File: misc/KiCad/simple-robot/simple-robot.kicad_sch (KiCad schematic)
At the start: 70 parts, among them J1 MotLA, J10 Screw_Terminal_2_P5.00mm, J11 JST02 HC-SR04, J12 IR_RF, J13 IR_LF, J14 JST_GV, J15 JST RF_Logic, J16 JST RF_PWR, J2 MotLB, J3 JST03 Servo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

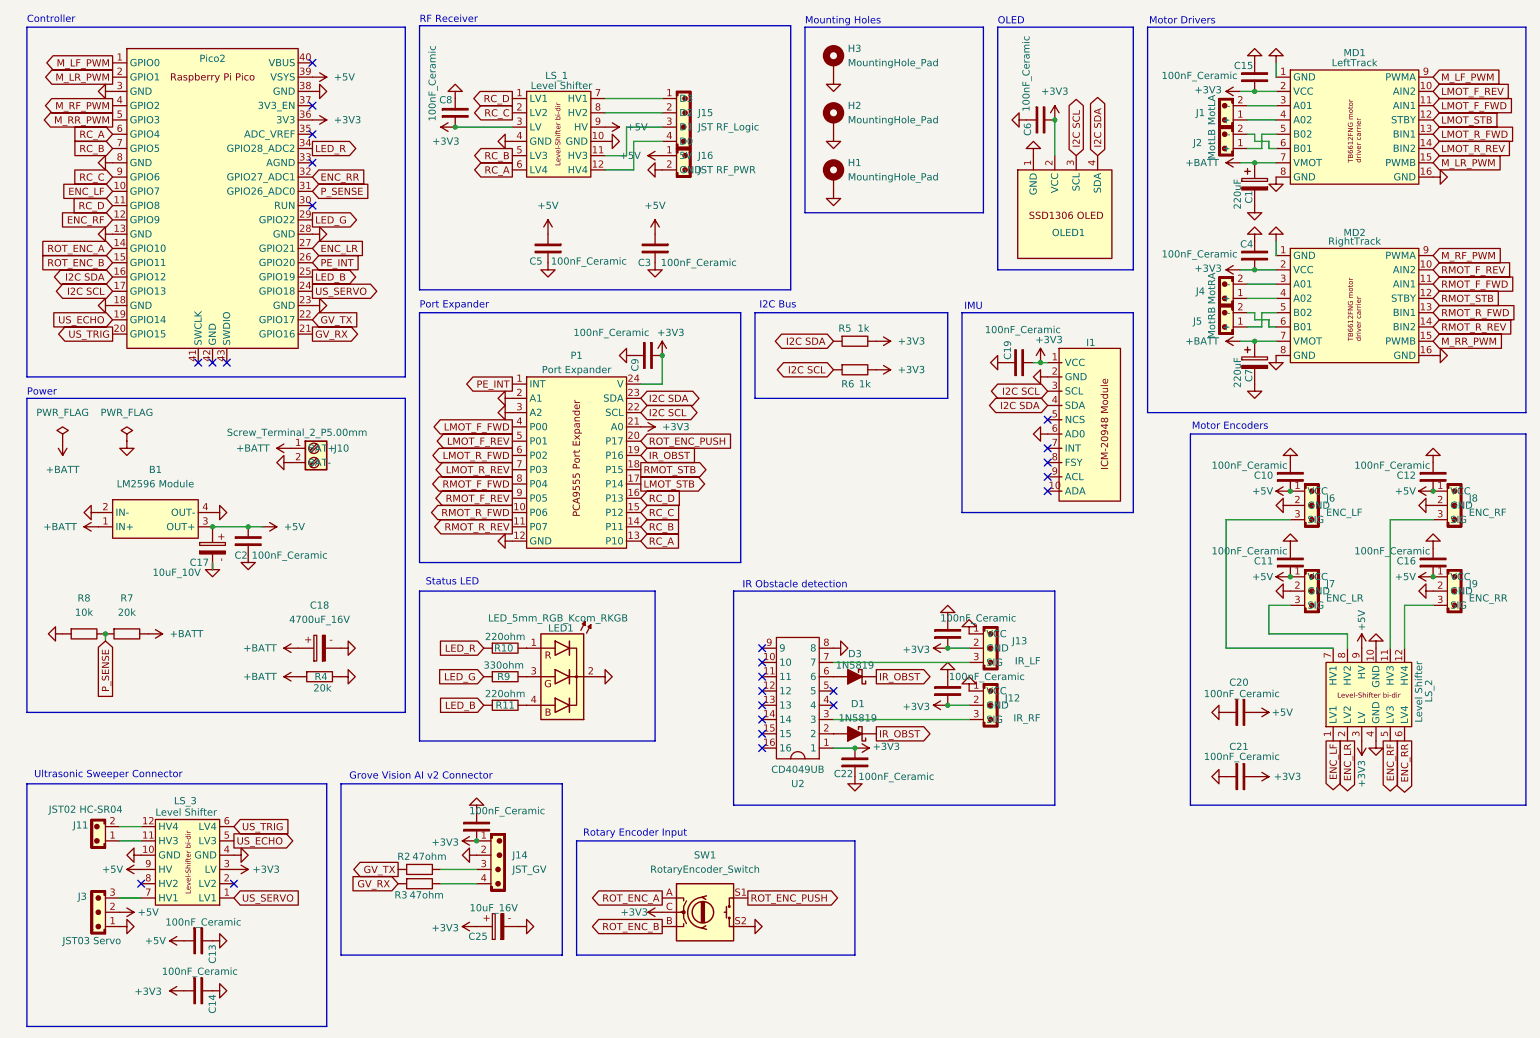
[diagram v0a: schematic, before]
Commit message: Update PCB layout: move footprints and pads
Update fp-info-cache (new hash) and add PCA9555 entry
Reposition many footprints and adjust silk text rotations/UUIDs
Change pad defaults (drill 2.8, width 3.2) and board prefs
(active layer and visible layers)
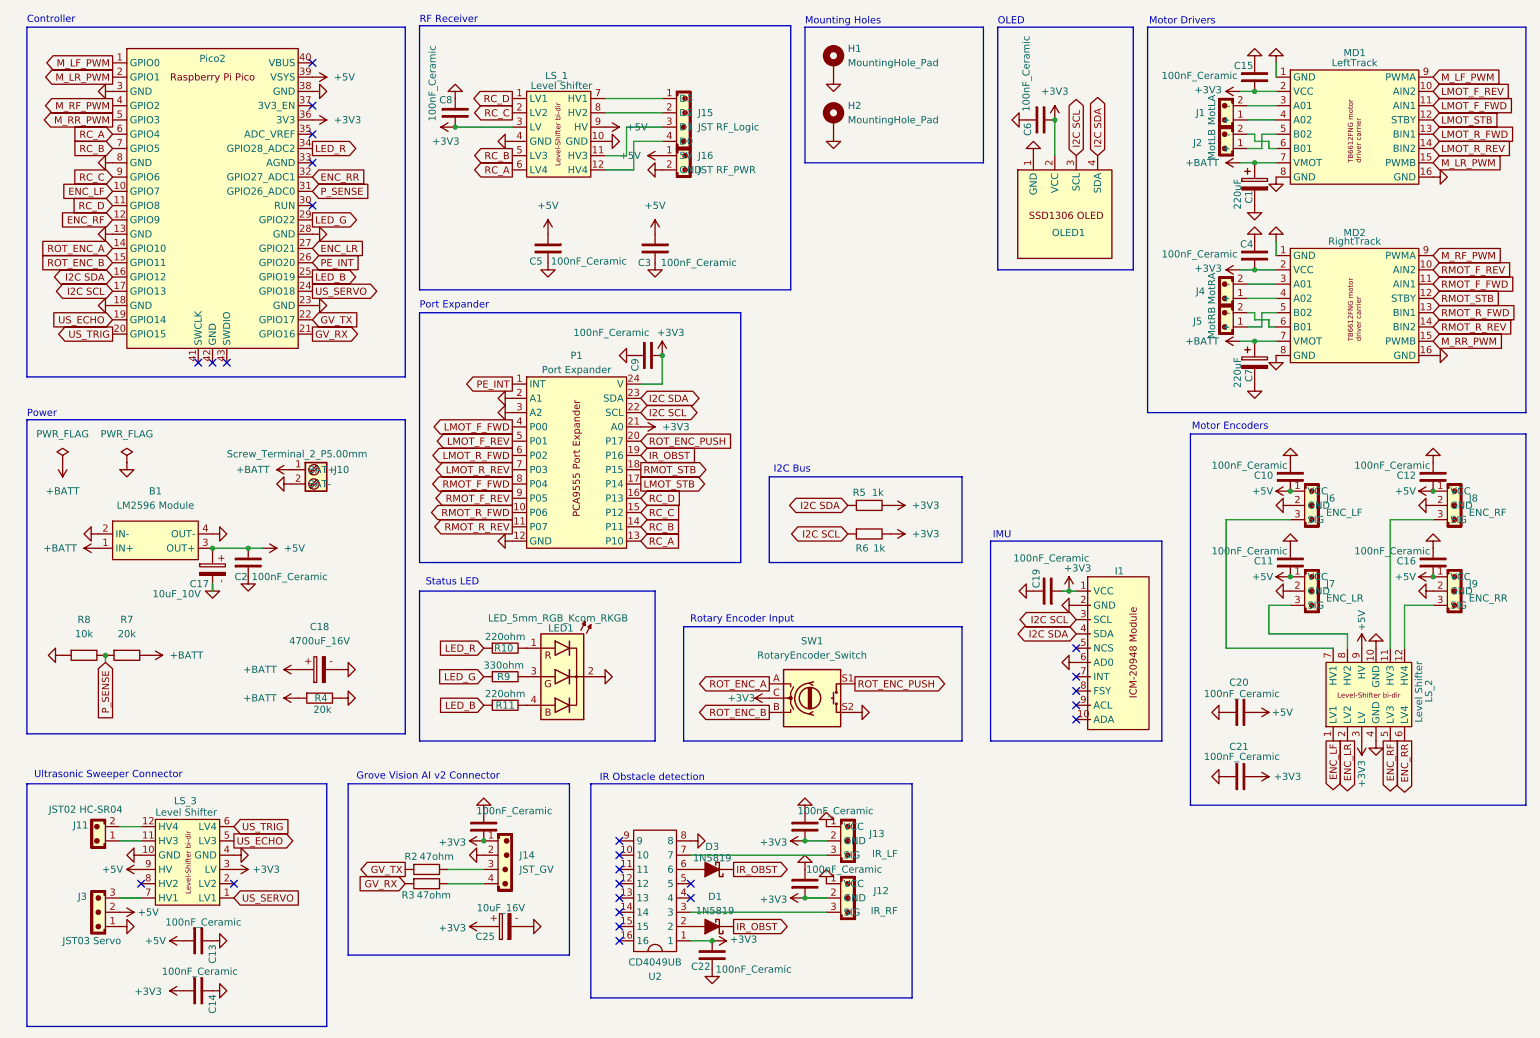
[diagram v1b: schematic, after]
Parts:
- removed H3: MountingHole_Pad, MountingHole:MountingHole_3.7mm_Pad_Via, symbol Mechanical:MountingHole_Pad
- P1: footprint (none) -> common-hobby-things:PCA9555 Port Expander
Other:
- moved on the sheet: B1, C17, C18, C19, C2, C22, C25, D1, D3, H1, I1, J10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

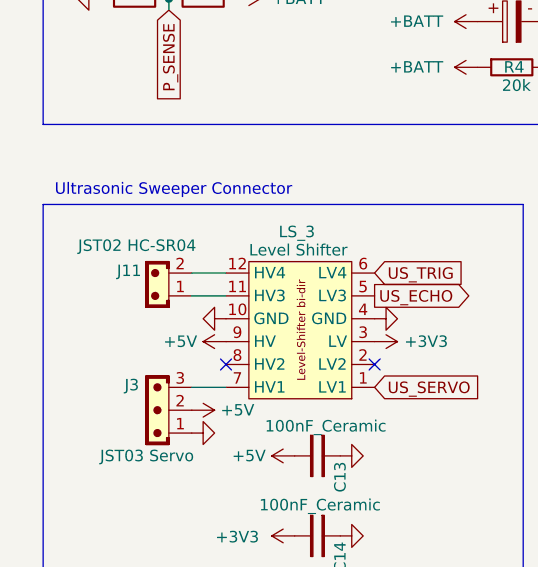
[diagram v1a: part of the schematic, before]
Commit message: Replace 2-pin JST with 4-pin and reposition parts
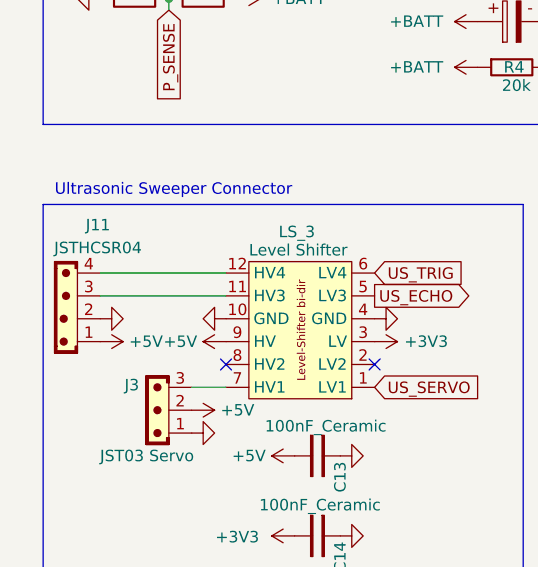
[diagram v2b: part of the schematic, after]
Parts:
- removed J11: JST02 HC-SR04, Connector_JST:JST_EH_B2B-EH-A_1x02_P2.50mm_Vertical, symbol PCM_SL_Connectors:JST_02
- added J11: JSTHCSR04, Connector_JST:JST_EH_B4B-EH-A_1x04_P2.50mm_Vertical, symbol PCM_SL_Connectors:JST_04
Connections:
- net +5V: now also J11.1
- net GND: now also J11.2
- net at LS_3.11 (HV3): now also J11.3
- net at LS_3.12 (HV4): now also J11.4
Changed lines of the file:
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@@
 	(wire
 		(pts
-			(xy 128.27 36.83) (xy 123.19 36.83)
+			(xy 21.59 161.29) (xy 35.56 161.29)
 		)
 		(stroke
@@
 	(wire
 		(pts
-			(xy 237.49 38.1) (xy 236.22 38.1)
+			(xy 128.27 36.83) (xy 123.19 36.83)
 		)
 		(stroke
@@
 	(wire
 		(pts
-			(xy 234.95 69.85) (xy 232.41 69.85)
+			(xy 237.49 38.1) (xy 236.22 38.1)
 		)
 		(stroke
@@
 	(wire
 		(pts
-			(xy 236.22 119.38) (xy 236.22 124.46)
+			(xy 234.95 69.85) (xy 232.41 69.85)
 		)
 		(stroke
@@
 	(wire
 		(pts
-			(xy 240.03 119.38) (xy 236.22 119.38)
+			(xy 236.22 119.38) (xy 236.22 124.46)
 		)
 		(stroke
@@
 	(wire
 		(pts
-			(xy 31.75 158.75) (xy 35.56 158.75)
+			(xy 240.03 119.38) (xy 236.22 119.38)
 		)
 		(stroke
@@
 	(wire
 		(pts
-			(xy 31.75 161.29) (xy 35.56 161.29)
-		)
-		(stroke
-			(width 0)
-			(type default)
-		)
-	)
-	(wire
-		(pts
 			(xy 250.19 124.46) (xy 250.19 127)
 		)
@@
 	(wire
 		(pts
+			(xy 21.59 158.75) (xy 35.56 158.75)
+		)
+		(stroke
+			(width 0)
+			(type default)
+		)
+	)
+	(wire
+		(pts
 			(xy 133.35 163.83) (xy 157.48 163.83)
 		)
@@
 	)
 	(symbol
-		(lib_name "JST_02_1")
-		(lib_id "PCM_SL_Connectors:JST_02")
-		(at 27.94 160.02 180)
-		(unit 1)
-		(exclude_from_sim no)
-		(in_bom yes)
-		(on_board yes)
-		(dnp no)
-		(property "Reference" "J11"
-			(at 26.162 158.496 0)
-			(effects
-				(font
-					(size 1.27 1.27)
-				)
-				(justify left)
-			)
-		)
-		(property "Value" "JST02 HC-SR04"
-			(at 32.258 155.702 0)
-			(effects
-				(font
-					(size 1.27 1.27)
-				)
-				(justify left)
-			)
-		)
-		(property "Footprint" "Connector_JST:JST_EH_B2B-EH-A_1x02_P2.50mm_Vertical"
-			(at 27.94 166.37 0)
-			(effects
-				(font
-					(size 1.27 1.27)
-				)
-				(hide yes)
-			)
-		)
-		(property "Datasheet" ""
-			(at 27.94 166.37 0)
-			(effects
-				(font
-					(size 1.27 1.27)
-				)
-				(hide yes)
-			)
-		)
-		(property "Description" "JST Connector  2 pins"
-			(at 27.94 160.02 0)
-			(effects
-				(font
-					(size 1.27 1.27)
-				)
-				(hide yes)
-			)
-		)
-		(pin "1"
-		)
-		(pin "2"
-		)
-		(instances
-			(project ""
-				(path "/bab01379-5d77-437e-95b1-5e737eb23384"
-					(reference "J11")
-					(unit 1)
-				)
-			)
-		)
-	)
-	(symbol
 		(lib_id "power:PWR_FLAG")
 		(at 33.02 93.98 0)
@@
 	)
 	(symbol
+		(lib_id "PCM_SL_Connectors:JST_04")
+		(at 17.78 162.306 180)
+		(unit 1)
+		(exclude_from_sim no)
+		(in_bom yes)
+		(on_board yes)
+		(dnp no)
+		(property "Reference" "J11"
+			(at 21.336 153.416 0)
+			(effects
+				(font
+					(size 1.27 1.27)
+				)
+			)
+		)
+		(property "Value" "JSTHCSR04"
+			(at 21.336 155.956 0)
+			(effects
+				(font
+					(size 1.27 1.27)
+				)
+			)
+		)
+		(property "Footprint" "Connector_JST:JST_EH_B4B-EH-A_1x04_P2.50mm_Vertical"
+			(at 17.78 171.45 0)
+			(effects
+				(font
+					(size 1.27 1.27)
+				)
+				(hide yes)
+			)
+		)
+		(property "Datasheet" ""
+			(at 17.78 171.45 0)
+			(effects
+				(font
+					(size 1.27 1.27)
+				)
+				(hide yes)
+			)
+		)
+		(property "Description" "JST Connector  4 pins"
+			(at 17.78 162.306 0)
+			(effects
+				(font
+					(size 1.27 1.27)
+				)
+				(hide yes)
+			)
+		)
+		(pin "3"
+		)
+		(pin "2"
+		)
+		(pin "1"
+		)
+		(pin "4"
+		)
+		(instances
+			(project "simple-robot"
+				(path "/bab01379-5d77-437e-95b1-5e737eb23384"
+					(reference "J11")
+					(unit 1)
+				)
+			)
+		)
+	)
+	(symbol
 		(lib_id "PCM_SL_Connectors:JST_02")
 		(at 228.6 63.5 180)
@@
 	)
 	(symbol
+		(lib_id "power:GND")
+		(at 21.59 163.83 90)
+		(unit 1)
+		(exclude_from_sim no)
+		(in_bom yes)
+		(on_board yes)
+		(dnp no)
+		(property "Reference" "#PWR0116"
+			(at 27.94 163.83 0)
+			(effects
+				(font
+					(size 1.27 1.27)
+				)
+				(hide yes)
+			)
+		)
+		(property "Value" "GND"
+			(at 24.892 163.83 0)
+			(effects
+				(font
+					(size 1.27 1.27)
+				)
+				(hide yes)
+			)
+		)
+		(property "Footprint" ""
+			(at 21.59 163.83 0)
+			(effects
+				(font
+					(size 1.27 1.27)
+				)
+				(hide yes)
+			)
+		)
+		(property "Datasheet" ""
+			(at 21.59 163.83 0)
+			(effects
+				(font
+					(size 1.27 1.27)
+				)
+				(hide yes)
+			)
+		)
+		(property "Description" "Power symbol creates a global label with name \"GND\" , ground"
+			(at 21.59 163.83 0)
+			(effects
+				(font
+					(size 1.27 1.27)
+				)
+				(hide yes)
+			)
+		)
+		(pin "1"
+		)
+		(instances
+			(project "simple-robot"
+				(path "/bab01379-5d77-437e-95b1-5e737eb23384"
+					(reference "#PWR0116")
+					(unit 1)
+				)
+			)
+		)
+	)
+	(symbol
 		(lib_id "PCM_SL_Capacitors:100nF_Ceramic")
 		(at 45.72 187.96 0)
@@
 					(unit 1)
 				)
+			)
+		)
+	)
+	(symbol
+		(lib_id "power:+5V")
+		(at 21.59 166.37 270)
+		(unit 1)
+		(exclude_from_sim no)
+		(in_bom yes)
+		(on_board yes)
+		(dnp no)
+		(property "Reference" "#PWR032"
+			(at 17.78 166.37 0)
+			(effects
+				(font
+					(size 1.27 1.27)
+				)
+				(hide yes)
+			)
+		)
+		(property "Value" "+5V"
+			(at 26.67 166.37 90)
+			(effects
+				(font
+					(size 1.27 1.27)
+				)
+			)
+		)
+		(property "Footprint" ""
+			(at 21.59 166.37 0)
+			(effects
+				(font
+					(size 1.27 1.27)
+				)
+				(hide yes)
+			)
+		)
+		(property "Datasheet" ""
+			(at 21.59 166.37 0)
+			(effects
+				(font
+					(size 1.27 1.27)
+				)
+				(hide yes)
+			)
+		)
+		(property "Description" "Power symbol creates a global label with name \"+5V\""
+			(at 21.59 166.37 0)
+			(effects
+				(font
+					(size 1.27 1.27)
+				)
+				(hide yes)
+			)
+		)
+		(pin "1"
+		)
+		(instances
+			(project "simple-robot"
+				(path "/bab01379-5d77-437e-95b1-5e737eb23384"
+					(reference "#PWR032")
+					(unit 1)
+				)

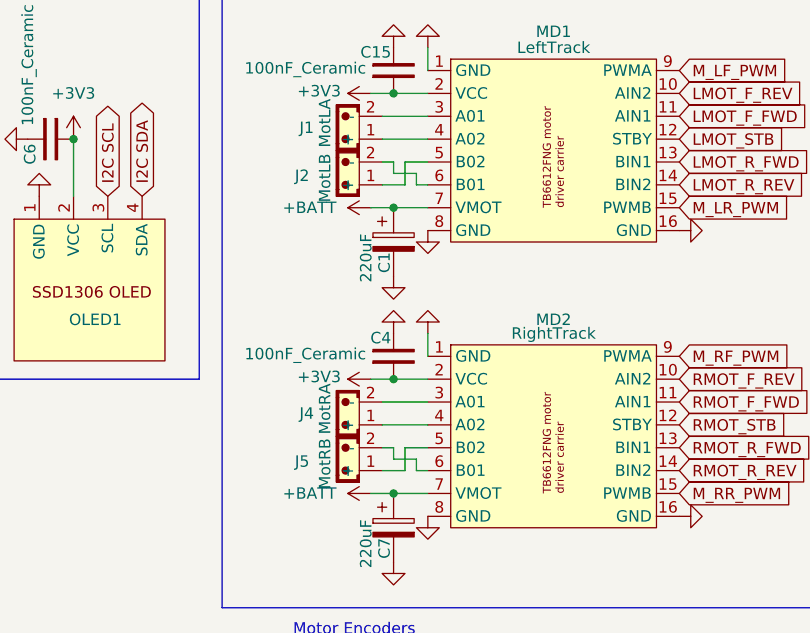
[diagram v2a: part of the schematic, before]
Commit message: pcb routing and some cleaning up; makingready for ordering the pcb mnufactured
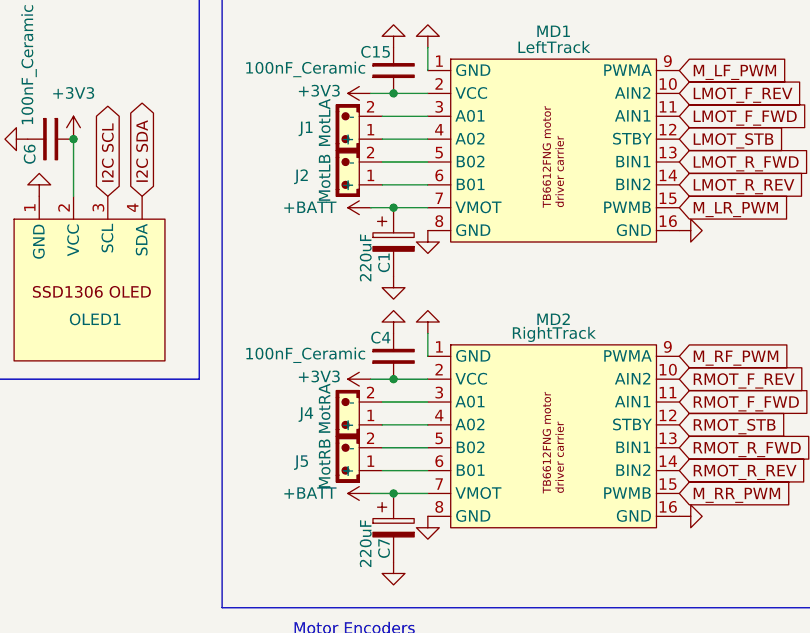
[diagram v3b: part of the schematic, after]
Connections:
- net at MD1.5 (B02): now also J2.2 (-); no longer J2.1 (+)
- net at MD1.6 (B01): now also J2.1 (+); no longer J2.2 (-)
- net at MD2.5 (B02): now also J5.2 (-); no longer J5.1 (+)
- net at MD2.6 (B01): now also J5.1 (+); no longer J5.2 (-)
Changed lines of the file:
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@@
 	(wire
 		(pts
-			(xy 234.95 38.1) (xy 232.41 38.1)
+			(xy 232.41 38.1) (xy 237.49 38.1)
 		)
 		(stroke
@@
 	(wire
 		(pts
-			(xy 236.22 38.1) (xy 236.22 36.83)
-		)
-		(stroke
-			(width 0)
-			(type default)
-		)
-	)
-	(wire
-		(pts
 			(xy 232.41 64.77) (xy 237.49 64.77)
 		)
@@
 	(wire
 		(pts
-			(xy 233.68 68.58) (xy 233.68 67.31)
-		)
-		(stroke
-			(width 0)
-			(type default)
-		)
-	)
-	(wire
-		(pts
 			(xy 90.17 166.37) (xy 96.52 166.37)
 		)
@@
 	(wire
 		(pts
-			(xy 236.22 36.83) (xy 233.68 36.83)
-		)
-		(stroke
-			(width 0)
-			(type default)
-		)
-	)
-	(wire
-		(pts
-			(xy 236.22 68.58) (xy 233.68 68.58)
-		)
-		(stroke
-			(width 0)
-			(type default)
-		)
-	)
-	(wire
-		(pts
 			(xy 232.41 30.48) (xy 237.49 30.48)
 		)
@@
 	(wire
 		(pts
-			(xy 233.68 67.31) (xy 232.41 67.31)
+			(xy 232.41 67.31) (xy 237.49 67.31)
 		)
 		(stroke
@@
 	(wire
 		(pts
-			(xy 233.68 35.56) (xy 232.41 35.56)
+			(xy 232.41 35.56) (xy 237.49 35.56)
 		)
 		(stroke
@@
 	(wire
 		(pts
-			(xy 234.95 67.31) (xy 234.95 69.85)
-		)
-		(stroke
-			(width 0)
-			(type default)
-		)
-	)
-	(wire
-		(pts
 			(xy 31.75 171.45) (xy 35.56 171.45)
 		)
@@
 	(wire
 		(pts
-			(xy 237.49 35.56) (xy 234.95 35.56)
-		)
-		(stroke
-			(width 0)
-			(type default)
-		)
-	)
-	(wire
-		(pts
 			(xy 200.66 116.84) (xy 201.93 116.84)
 		)
@@
 	(wire
 		(pts
-			(xy 237.49 38.1) (xy 236.22 38.1)
-		)
-		(stroke
-			(width 0)
-			(type default)
-		)
-	)
-	(wire
-		(pts
-			(xy 234.95 69.85) (xy 232.41 69.85)
+			(xy 232.41 69.85) (xy 237.49 69.85)
 		)
 		(stroke
@@
 	(wire
 		(pts
-			(xy 236.22 69.85) (xy 236.22 68.58)
-		)
-		(stroke
-			(width 0)
-			(type default)
-		)
-	)
-	(wire
-		(pts
 			(xy 91.44 34.29) (xy 101.6 34.29)
 		)
@@
 	(wire
 		(pts
-			(xy 234.95 35.56) (xy 234.95 38.1)
-		)
-		(stroke
-			(width 0)
-			(type default)
-		)
-	)
-	(wire
-		(pts
 			(xy 228.6 104.14) (xy 228.6 127)
 		)
@@
 	(wire
 		(pts
-			(xy 233.68 36.83) (xy 233.68 35.56)
-		)
-		(stroke
-			(width 0)
-			(type default)
-		)
-	)
-	(wire
-		(pts
 			(xy 260.35 119.38) (xy 260.35 127)
 		)
@@
 	(wire
 		(pts
-			(xy 237.49 69.85) (xy 236.22 69.85)
-		)
-		(stroke
-			(width 0)
-			(type default)
-		)
-	)
-	(wire
-		(pts
 			(xy 233.68 59.69) (xy 237.49 59.69)
 		)
@@
 		)
 		(stroke
-			(width 0)
-			(type default)
-		)
-	)
-	(wire
-		(pts
-			(xy 237.49 67.31) (xy 234.95 67.31)
-		)
-		(stroke
